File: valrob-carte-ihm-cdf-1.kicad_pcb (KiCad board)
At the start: 2 copper layers, 55 x 75 mm, 85 parts, among them J1 USB_C_Receptacle_USB2.0_14P, J2 Conn_01x02, J3 Conn_01x02, J4 Conn_01x04_Pin, J5 Conn_01x04_Pin, J6 Conn_01x04_Pin, SW1 SW_Push, SW2 SW_Push, SW3 SW_DIP_x04, SW4 SW_SPDT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

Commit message: pcb: add USB routing
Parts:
- moved R2 0.25 mm to (123.0, 78.0)
- moved R8 0.25 mm to (140.0, 86.0)
- moved R9 0.25 mm to (140.0, 84.8)
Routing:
- net Net-(J1-CC2): track 0.00 -> 21.8 mm
- net VBUS: track 0.00 -> 17.3 mm
- net Net-(J1-CC1): track 0.00 -> 7.73 mm, vias 0 -> 2
- net Net-(J1-D+-PadA6): track 0.00 -> 7.64 mm
- net /D+: track 0.00 -> 7.10 mm
- net /D-: track 0.00 -> 7.00 mm
- net Net-(J1-D--PadA7): track 0.00 -> 5.45 mm
- net +5V: track 0.00 -> 4.58 mm
- net GND: track 0.00 -> 3.96 mm, vias 57 -> 59
- net /ESP_D+: track 0.00 -> 3.83 mm
- net /ESP_D-: track 0.00 -> 3.69 mm

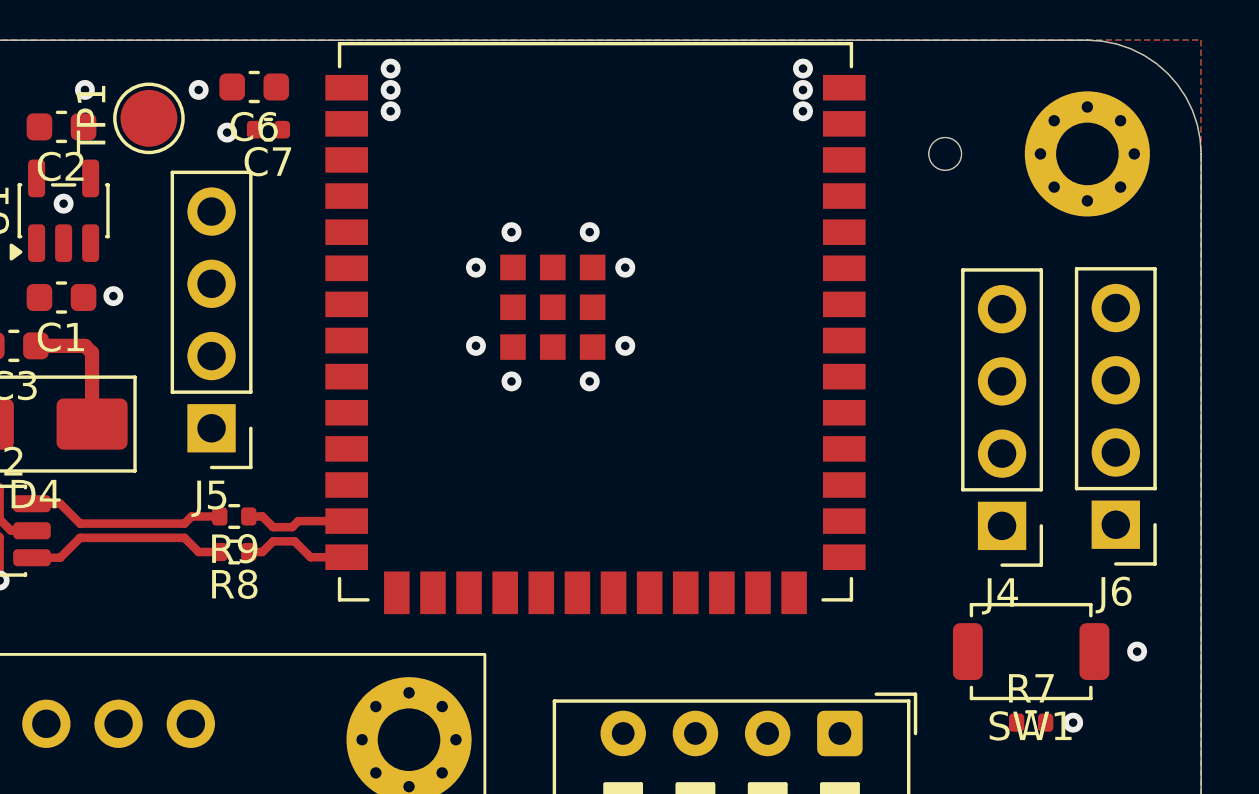
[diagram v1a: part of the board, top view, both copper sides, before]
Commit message: pcb: add UART routing
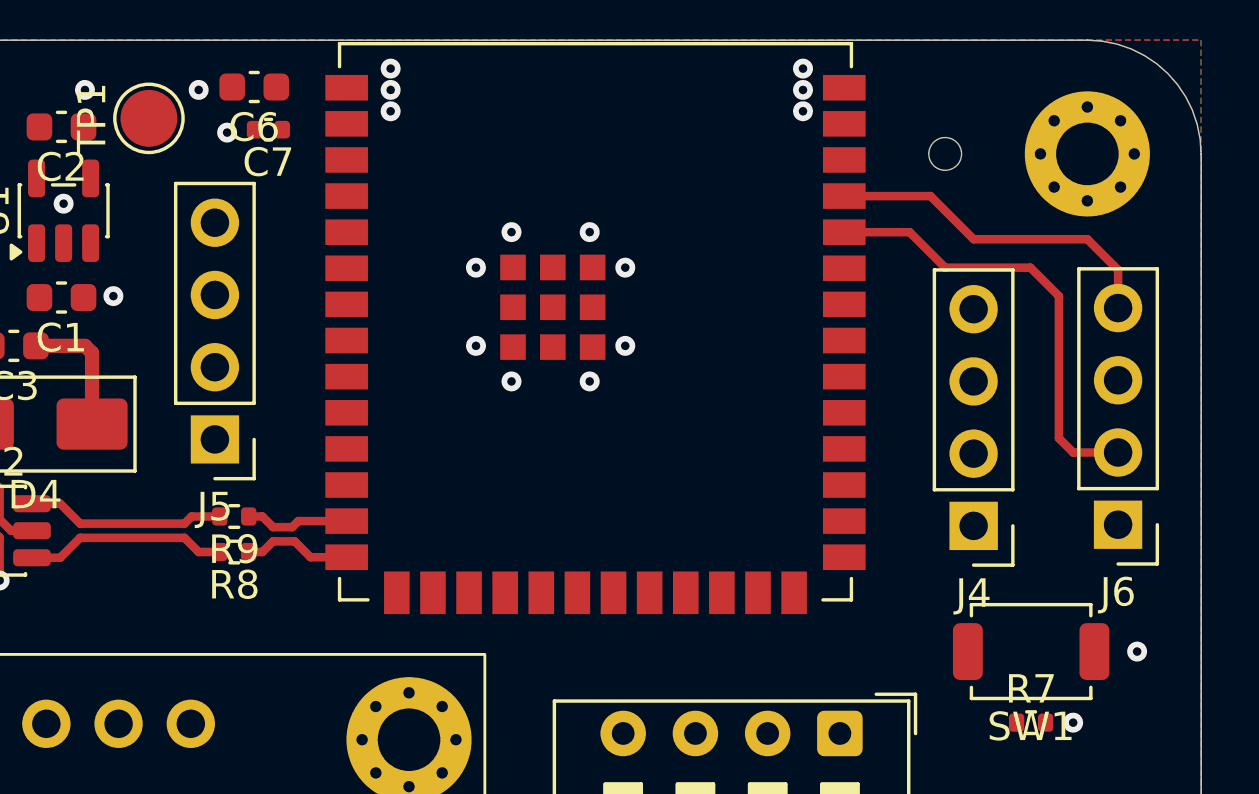
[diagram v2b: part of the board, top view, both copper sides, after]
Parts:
- moved J4 1.00 mm to (166.0, 85.1)
- moved J5 0.41 mm to (139.3, 82.0)
- moved J6 0.08 mm to (171.1, 85.0)
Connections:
- U4 pad 12: /SCL -> unconnected-(U4-GPIO8/TOUCH8/ADC1_CH7/SUBSPICS1-Pad12)
- U4 pad 15: /RGB_LEDS -> /SCL
- U4 pad 18: unconnected-(U4-GPIO10/TOUCH10/ADC1_CH9/FSPICS0/FSPIIO4/SUBSPICS0-Pad18) -> /RGB_LEDS
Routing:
- net /U0RXD: track 0.00 -> 15.8 mm
- net /U0TXD: track 0.00 -> 12.0 mm
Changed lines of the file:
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@@
 	(net 58 "/Switches/ESW5")
 	(net 59 "/Switches/ESW2")
-	(net 60 "unconnected-(U4-GPIO10{slash}TOUCH10{slash}ADC1_CH9{slash}FSPICS0{slash}FSPIIO4{slash}SUBSPICS0-Pad18)")
-	(net 61 "unconnected-(U4-GPIO16{slash}U0CTS{slash}ADC2_CH5{slash}XTAL_32K_N-Pad9)")
-	(net 62 "/Switches/ESW6")
-	(net 63 "Net-(U4-GPIO21)")
-	(net 64 "Net-(U4-GPIO47{slash}SPICLK_P{slash}SUBSPICLK_P_DIFF)")
-	(net 65 "unconnected-(U4-GPIO46-Pad16)")
+	(net 60 "unconnected-(U4-GPIO16{slash}U0CTS{slash}ADC2_CH5{slash}XTAL_32K_N-Pad9)")
+	(net 61 "/Switches/ESW6")
+	(net 62 "Net-(U4-GPIO21)")
+	(net 63 "Net-(U4-GPIO47{slash}SPICLK_P{slash}SUBSPICLK_P_DIFF)")
+	(net 64 "unconnected-(U4-GPIO46-Pad16)")
+	(net 65 "unconnected-(U4-GPIO8{slash}TOUCH8{slash}ADC1_CH7{slash}SUBSPICS1-Pad12)")
 	(footprint "Diode_SMD:D_SMB"
 		(layer "F.Cu")
@@
 			(layers "F.Cu" "F.Mask" "F.Paste")
 			(roundrect_rratio 0.25)
-			(net 62 "/Switches/ESW6")
+			(net 61 "/Switches/ESW6")
 			(pintype "output")
 		)
@@
 	(footprint "Connector_PinHeader_2.54mm:PinHeader_1x04_P2.54mm_Vertical"
 		(layer "F.Cu")
-		(at 139.2025 81.6475 180)
+		(at 139.32 82.04 180)
 		(descr "Through hole straight pin header, 1x04, 2.54mm pitch, single row")
 		(tags "Through hole pin header THT 1x04 2.54mm single row")
@@
 	(footprint "Connector_PinHeader_2.54mm:PinHeader_1x04_P2.54mm_Vertical"
 		(layer "F.Cu")
-		(at 171 85.04 180)
+		(at 171.08 85.04 180)
 		(descr "Through hole straight pin header, 1x04, 2.54mm pitch, single row")
 		(tags "Through hole pin header THT 1x04 2.54mm single row")
@@
 	(footprint "Connector_PinHeader_2.54mm:PinHeader_1x04_P2.54mm_Vertical"
 		(layer "F.Cu")
-		(at 167 85.08 180)
+		(at 166 85.08 180)
 		(descr "Through hole straight pin header, 1x04, 2.54mm pitch, single row")
 		(tags "Through hole pin header THT 1x04 2.54mm single row")
@@
 			(size 1.5 0.9)
 			(layers "F.Cu" "F.Mask" "F.Paste")
-			(net 61 "unconnected-(U4-GPIO16{slash}U0CTS{slash}ADC2_CH5{slash}XTAL_32K_N-Pad9)")
+			(net 60 "unconnected-(U4-GPIO16{slash}U0CTS{slash}ADC2_CH5{slash}XTAL_32K_N-Pad9)")
 			(pinfunction "GPIO16/U0CTS/ADC2_CH5/XTAL_32K_N")
 			(pintype "bidirectional+no_connect")
@@
 			(size 1.5 0.9)
 			(layers "F.Cu" "F.Mask" "F.Paste")
-			(net 62 "/Switches/ESW6")
+			(net 61 "/Switches/ESW6")
 			(pinfunction "GPIO18/U1RXD/ADC2_CH7/CLK_OUT3")
 			(pintype "bidirectional")
@@
 			(size 1.5 0.9)
 			(layers "F.Cu" "F.Mask" "F.Paste")
-			(net 48 "/SCL")
+			(net 65 "unconnected-(U4-GPIO8{slash}TOUCH8{slash}ADC1_CH7{slash}SUBSPICS1-Pad12)")
 			(pinfunction "GPIO8/TOUCH8/ADC1_CH7/SUBSPICS1")
-			(pintype "bidirectional")
+			(pintype "bidirectional+no_connect")
 		)
 		(pad "13" smd rect
@@
 			(size 1.5 0.9)
 			(layers "F.Cu" "F.Mask" "F.Paste")
-			(net 13 "/RGB_LEDS")
+			(net 48 "/SCL")
 			(pinfunction "GPIO3/TOUCH3/ADC1_CH2")
 			(pintype "bidirectional")
@@
 			(size 1.5 0.9)
 			(layers "F.Cu" "F.Mask" "F.Paste")
-			(net 65 "unconnected-(U4-GPIO46-Pad16)")
+			(net 64 "unconnected-(U4-GPIO46-Pad16)")
 			(pinfunction "GPIO46")
 			(pintype "bidirectional")
@@
 			(size 1.5 0.9)
 			(layers "F.Cu" "F.Mask" "F.Paste")
-			(net 60 "unconnected-(U4-GPIO10{slash}TOUCH10{slash}ADC1_CH9{slash}FSPICS0{slash}FSPIIO4{slash}SUBSPICS0-Pad18)")
+			(net 13 "/RGB_LEDS")
 			(pinfunction "GPIO10/TOUCH10/ADC1_CH9/FSPICS0/FSPIIO4/SUBSPICS0")
-			(pintype "bidirectional+no_connect")
+			(pintype "bidirectional")
 		)
 		(pad "19" smd rect
@@
 			(size 1.5 0.9)
 			(layers "F.Cu" "F.Mask" "F.Paste")
-			(net 63 "Net-(U4-GPIO21)")
+			(net 62 "Net-(U4-GPIO21)")
 			(pinfunction "GPIO21")
 			(pintype "bidirectional")
@@
 			(size 1.5 0.9)
 			(layers "F.Cu" "F.Mask" "F.Paste")
-			(net 64 "Net-(U4-GPIO47{slash}SPICLK_P{slash}SUBSPICLK_P_DIFF)")
+			(net 63 "Net-(U4-GPIO47{slash}SPICLK_P{slash}SUBSPICLK_P_DIFF)")
 			(pinfunction "GPIO47/SPICLK_P/SUBSPICLK_P_DIFF")
 			(pintype "bidirectional")
@@
 			(layers "*.Cu" "*.Mask")
 			(remove_unused_layers no)
-			(net 64 "Net-(U4-GPIO47{slash}SPICLK_P{slash}SUBSPICLK_P_DIFF)")
+			(net 63 "Net-(U4-GPIO47{slash}SPICLK_P{slash}SUBSPICLK_P_DIFF)")
 			(pintype "passive")
 		)
@@
 			(layers "*.Cu" "*.Mask")
 			(remove_unused_layers no)
-			(net 63 "Net-(U4-GPIO21)")
+			(net 62 "Net-(U4-GPIO21)")
 			(pintype "passive")
 		)
@@
 	)
 	(segment
+		(start 164.4825 73.4825)
+		(end 161.4525 73.4825)
+		(width 0.3)
+		(layer "F.Cu")
+		(net 37)
+	)
+	(segment
+		(start 171.08 76.08)
+		(end 170 75)
+		(width 0.3)
+		(layer "F.Cu")
+		(net 37)
+	)
+	(segment
+		(start 171.08 77.42)
+		(end 171.08 76.08)
+		(width 0.3)
+		(layer "F.Cu")
+		(net 37)
+	)
+	(segment
+		(start 166 75)
+		(end 164.4825 73.4825)
+		(width 0.3)
+		(layer "F.Cu")
+		(net 37)
+	)
+	(segment
+		(start 170 75)
+		(end 166 75)
+		(width 0.3)
+		(layer "F.Cu")
+		(net 37)
+	)
+	(segment
+		(start 165 76)
+		(end 163.7525 74.7525)
+		(width 0.3)
+		(layer "F.Cu")
+		(net 38)
+	)
+	(segment
+		(start 169.5 82.5)
+		(end 169 82)
+		(width 0.3)
+		(layer "F.Cu")
+		(net 38)
+	)
+	(segment
+		(start 168 76)
+		(end 165 76)
+		(width 0.3)
+		(layer "F.Cu")
+		(net 38)
+	)
+	(segment
+		(start 169 82)
+		(end 169 77)
+		(width 0.3)
+		(layer "F.Cu")
+		(net 38)
+	)
+	(segment
+		(start 163.7525 74.7525)
+		(end 161.4525 74.7525)
+		(width 0.3)
+		(layer "F.Cu")
+		(net 38)
+	)
+	(segment
+		(start 171.08 82.5)
+		(end 169.5 82.5)
+		(width 0.3)
+		(layer "F.Cu")
+		(net 38)
+	)
+	(segment
+		(start 169 77)
+		(end 168 76)
+		(width 0.3)
+		(layer "F.Cu")
+		(net 38)
+	)
+	(segment

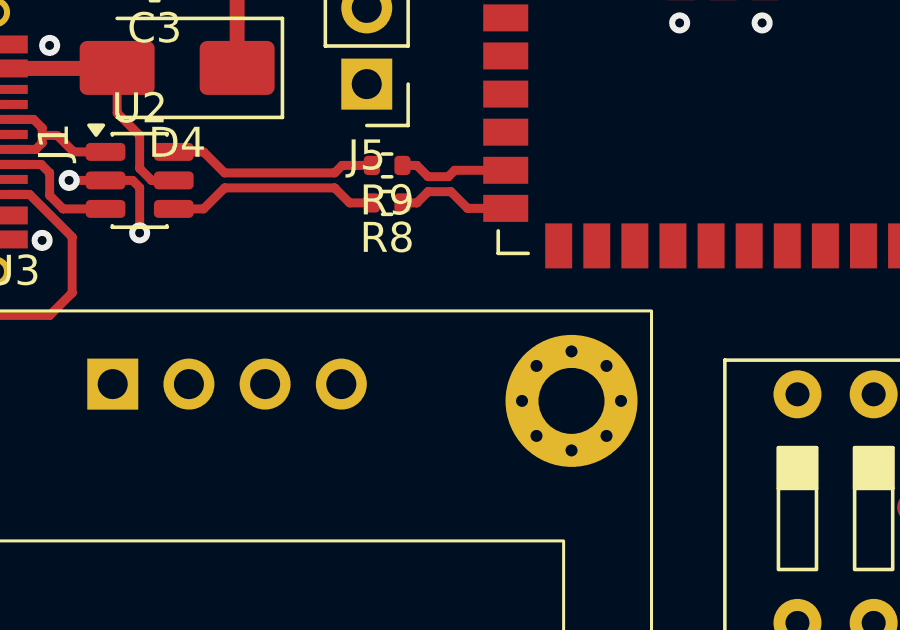
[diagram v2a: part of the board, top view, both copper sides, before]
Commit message: pcb: add I2C display routing
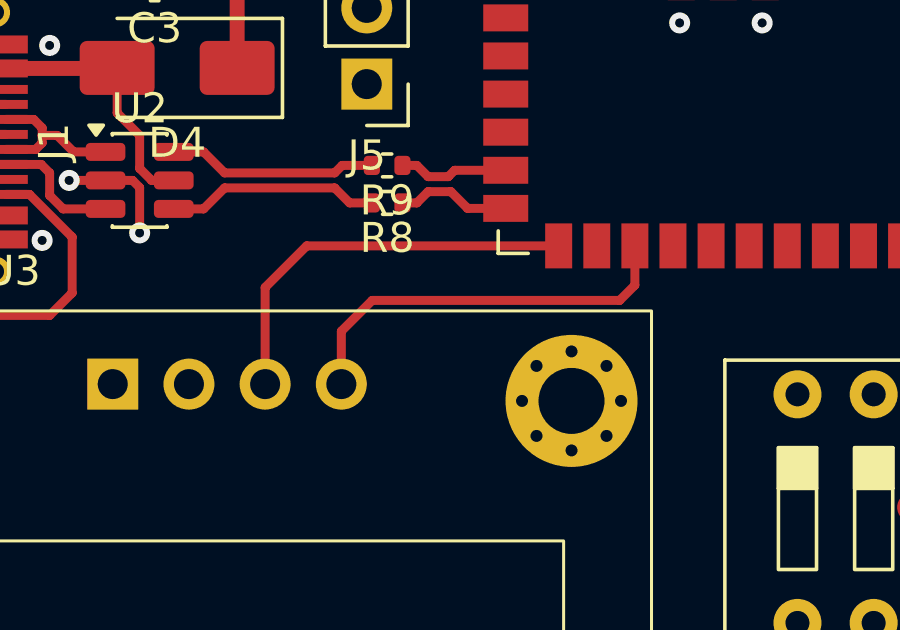
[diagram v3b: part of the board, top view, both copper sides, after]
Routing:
- net /SCL: track 0.00 -> 13.6 mm
- net /SDA: track 0.00 -> 13.5 mm
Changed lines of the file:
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@@
 		(net 43)
+	)
+	(segment
+		(start 137.3175 87.4325)
+		(end 145.7175 87.4325)
+		(width 0.3)
+		(layer "F.Cu")
+		(net 48)
+	)
+	(segment
+		(start 135.9325 88.8175)
+		(end 137.3175 87.4325)
+		(width 0.3)
+		(layer "F.Cu")
+		(net 48)
+	)
+	(segment
+		(start 135.9325 92.04)
+		(end 135.9325 88.8175)
+		(width 0.3)
+		(layer "F.Cu")
+		(net 48)
+	)
+	(segment
+		(start 139.5 89.25)
+		(end 147.75 89.25)
+		(width 0.3)
+		(layer "F.Cu")
+		(net 49)
+	)
+	(segment
+		(start 138.4725 92.04)
+		(end 138.4725 90.2775)
+		(width 0.3)
+		(layer "F.Cu")
+		(net 49)
+	)
+	(segment
+		(start 138.4725 90.2775)
+		(end 139.5 89.25)
+		(width 0.3)
+		(layer "F.Cu")
+		(net 49)
+	)
+	(segment
+		(start 148.2575 88.7425)
+		(end 148.2575 87.4325)
+		(width 0.3)
+		(layer "F.Cu")
+		(net 49)
+	)
+	(segment
+		(start 147.75 89.25)
+		(end 148.2575 88.7425)
+		(width 0.3)
+		(layer "F.Cu")
+		(net 49)
 	)
 	(zone

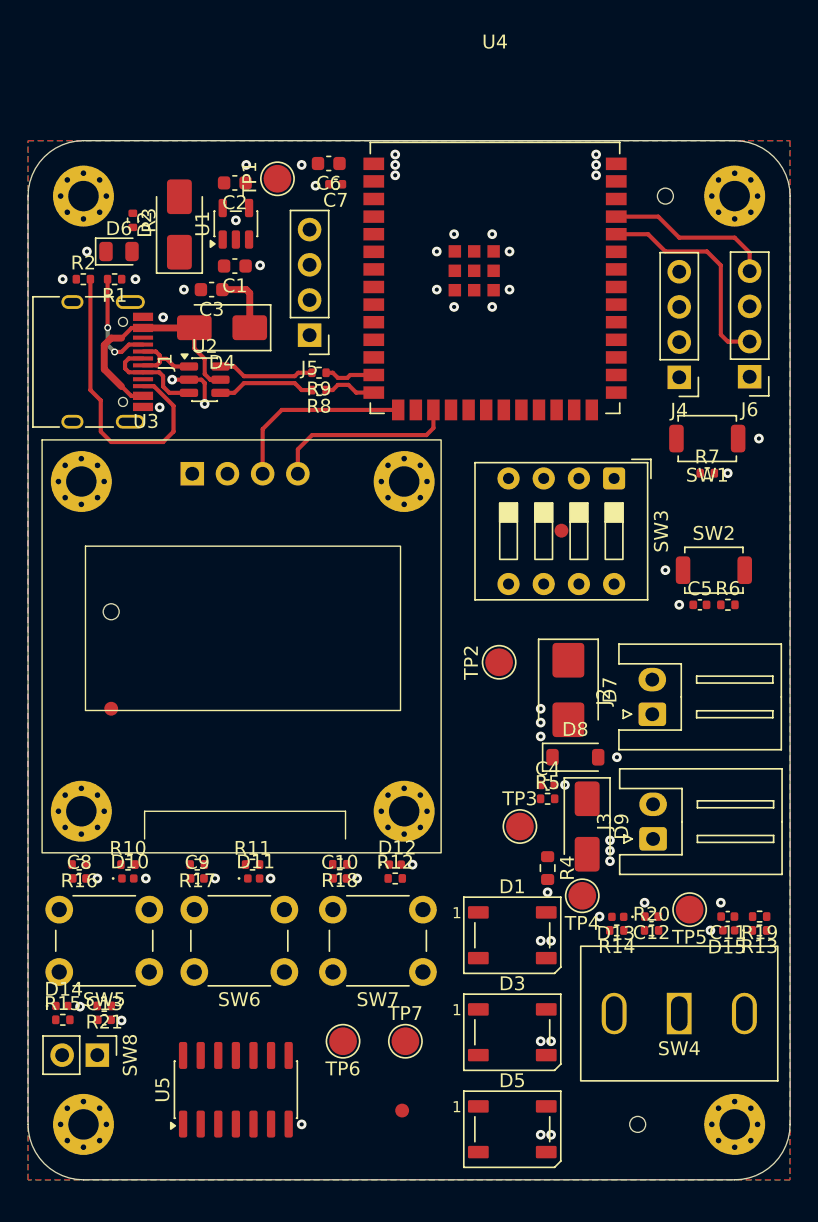
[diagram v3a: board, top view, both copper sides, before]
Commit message: pcb: add display buttons routing
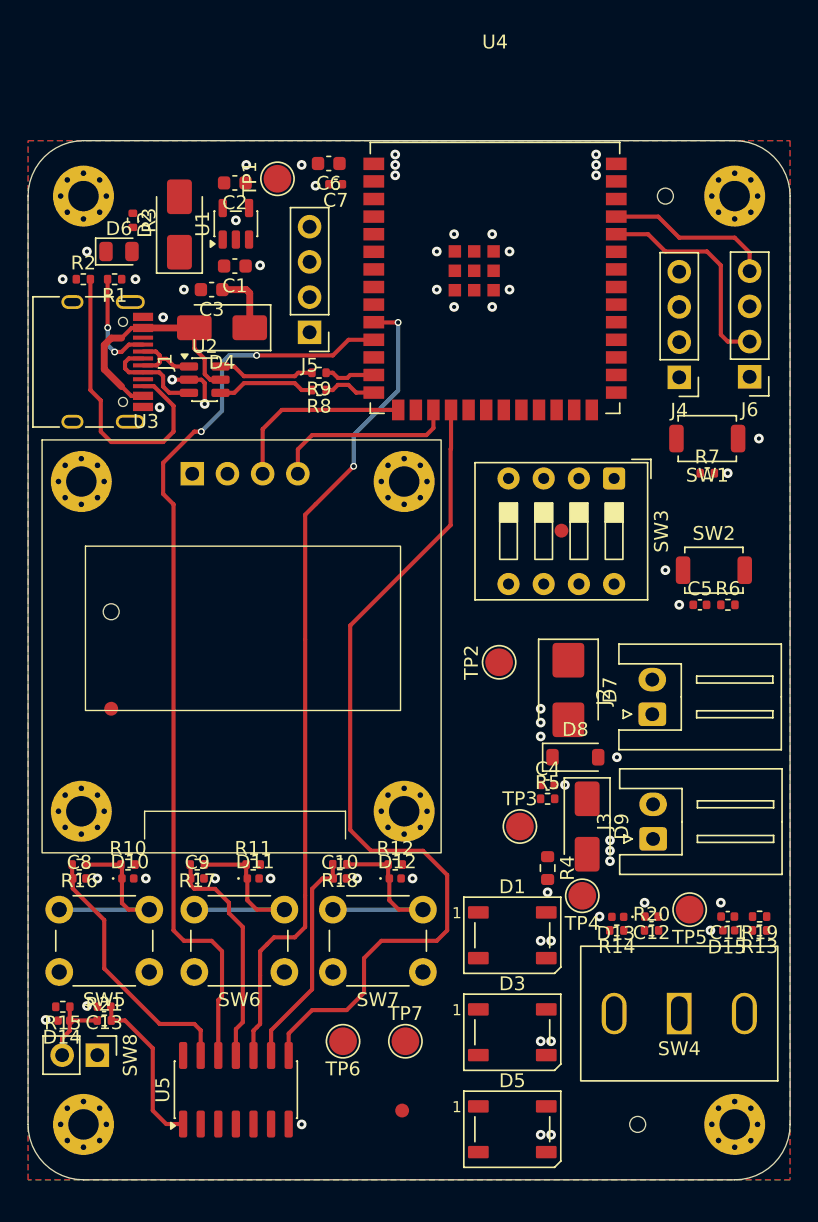
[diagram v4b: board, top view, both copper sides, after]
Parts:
- moved D14 1.07 mm to (121.6, 131.5), turned to 180 degrees
- moved R21 1.05 mm to (124.5, 131.5), turned to 0 degrees
- moved D12 1.00 mm to (145.5, 121.2)
- moved R12 1.00 mm to (145.5, 120.2)
- moved C13 0.95 mm to (124.5, 130.5), turned to 180 degrees
- moved R15 0.94 mm to (121.5, 130.5), turned to 180 degrees
- moved J5 0.21 mm to (139.3, 81.8)
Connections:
- U4 pad 18: /RGB_LEDS -> /Switches/ESW4
- U4 pad 22: /Switches/ESW4 -> /RGB_LEDS
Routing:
- net /Switches/ESW6: track 0.00 -> 66.7 mm, vias 0 -> 2
- net /Switches/ESW4: track 0.00 -> 63.2 mm
- net /Switches/ESW5: track 0.00 -> 59.9 mm, vias 0 -> 2
- net Net-(C8-Pad1): track 0.00 -> 19.1 mm
- net Net-(C9-Pad1): track 0.00 -> 16.4 mm
- net Net-(C10-Pad1): track 0.00 -> 16.1 mm
- net Net-(D11-K): track 0.00 -> 15.0 mm
- net Net-(D12-K): track 0.00 -> 14.8 mm
- net Net-(D10-K): track 0.00 -> 14.0 mm
- net Net-(C13-Pad1): track 0.00 -> 11.9 mm
- net Net-(D14-K): track 0.00 -> 5.71 mm

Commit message: pcb: add toggle switch routing
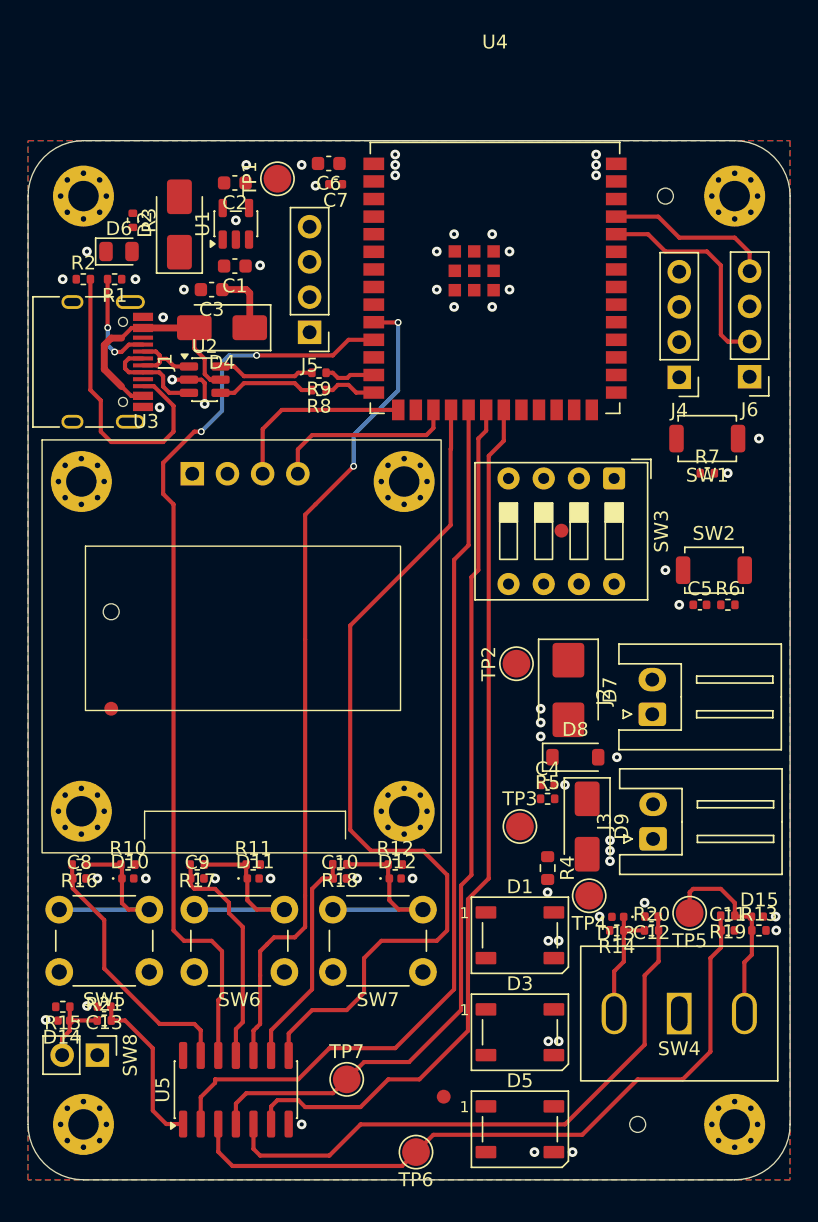
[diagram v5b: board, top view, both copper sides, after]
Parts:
- moved TP6 9.58 mm to (147.0, 141.0)
- moved TP7 5.05 mm to (142.0, 135.8)
- moved REF** 3.16 mm to (149.0, 137.0)
- moved R19 2.30 mm to (169.5, 123.9)
- moved D15 2.29 mm to (171.6, 124.0), turned to 0 degrees
- moved TP2 1.25 mm to (154.2, 105.8)
- moved C11 1.00 mm to (169.5, 125.0), turned to 0 degrees
- moved D1 0.55 mm to (154.5, 125.3)
- moved D3 0.55 mm to (154.5, 132.3)
- moved D5 0.55 mm to (154.5, 139.3)
- moved TP4 0.50 mm to (159.5, 122.5)
- moved TP5 0.25 mm to (166.8, 123.8)
- turned R13 to 0 degrees
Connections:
- U4 pad 20: /Switches/ESW2 -> /Switches/ESW3
- U4 pad 21: /Switches/ESW3 -> /Switches/ESW2
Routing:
- net /Switches/ESW1: track 0.00 -> 65.8 mm
- net /Switches/ESW3: track 0.00 -> 64.6 mm
- net /Switches/ESW2: track 0.00 -> 64.0 mm
- net Net-(C11-Pad1): track 0.00 -> 51.5 mm
- net Net-(C12-Pad1): track 0.00 -> 43.2 mm
- net Net-(D15-K): track 0.00 -> 14.4 mm
- net Net-(D13-K): track 0.00 -> 8.76 mm
